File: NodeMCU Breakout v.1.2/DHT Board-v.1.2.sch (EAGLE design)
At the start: 17 parts, among them IC1 74HCT125N

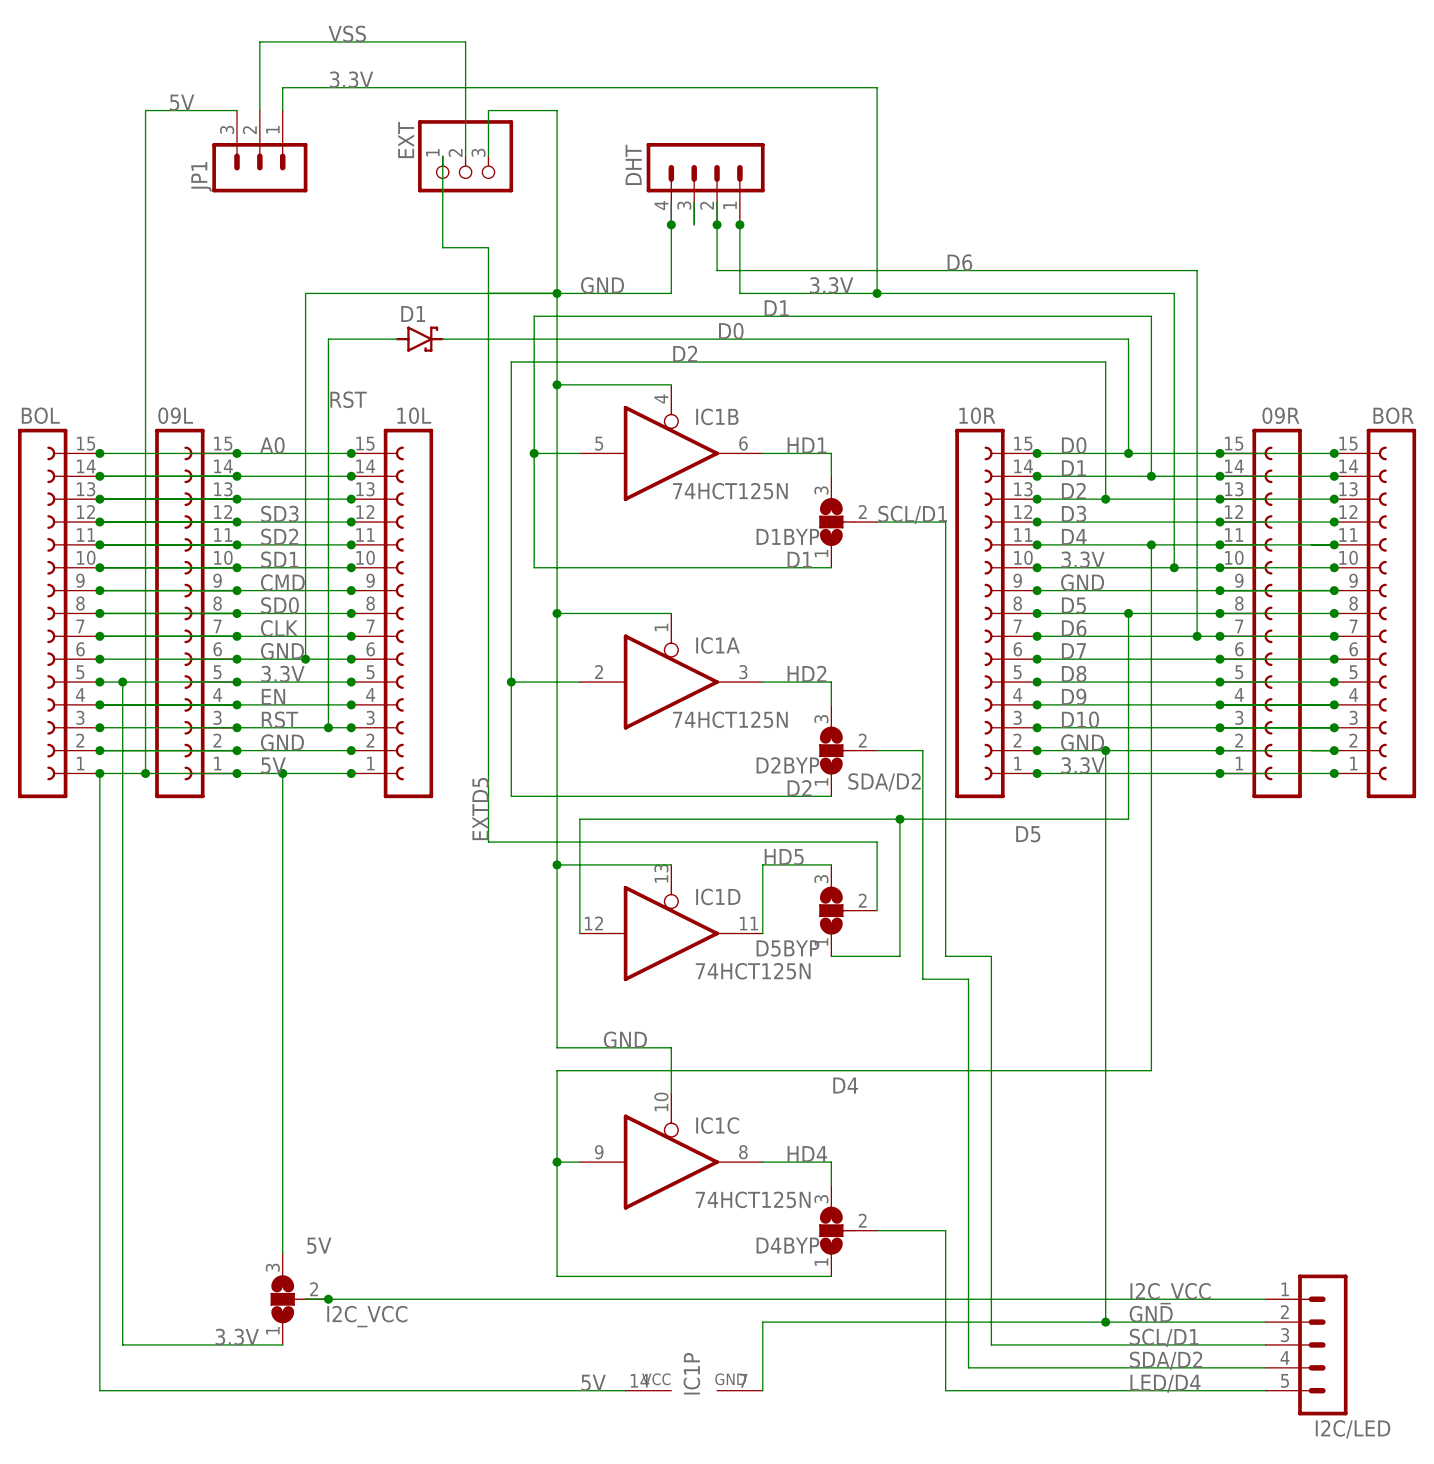
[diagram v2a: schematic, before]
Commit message: 2/2/19(BK): Updated rev 1.2 to final:
-Removed I2C_VCC Solder jumper and added 6th pin to the header (both 3.3v & 5v are brought out)
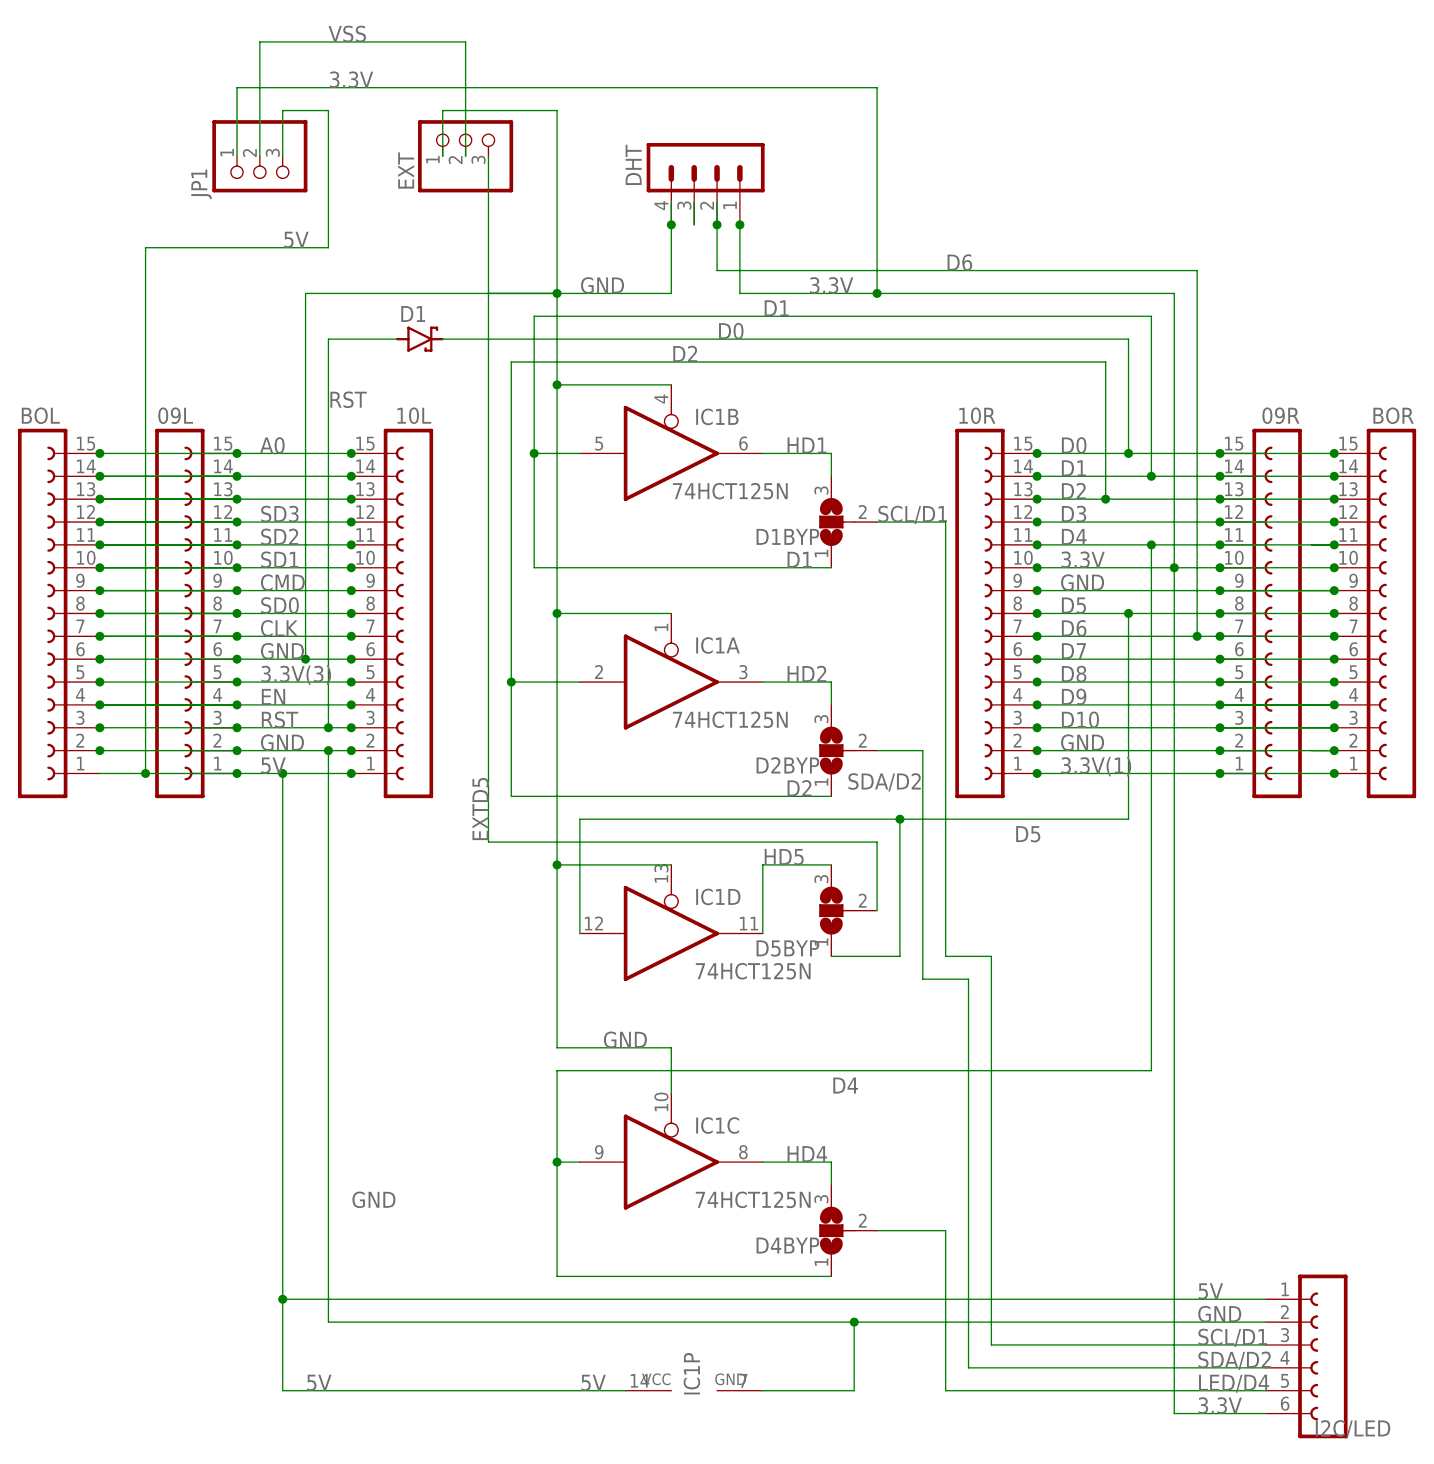
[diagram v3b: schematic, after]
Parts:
- removed I2C_VCC: (no value), jumper:SJ2W
- EXT: device pinhead:PINHD-1X3 -> pinhead:PINHD-1X3/90
- I2C/LED: device con-lstb:MA05-1 -> con-lsta:FE06-1
- JP1: device con-lstb:MA03-1 -> pinhead:PINHD-1X3
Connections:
- removed net I2C_VCC: I2C/LED.1, I2C_VCC.2
- new net 3.3V(1): 09R.1, 10R.1, BOR.1
- new net 3.3V(3): 09L.5, 10L.5, BOL.5
- net 3.3V: now also I2C/LED.6; no longer 09L.5, 09R.1, 10L.5, 10R.1, BOL.5, BOR.1, I2C_VCC.1
- net 5V: now also I2C/LED.1; no longer I2C_VCC.3
- net EXTD5: now also EXT.3; no longer EXT.1
- net GND: now also EXT.1; no longer EXT.3
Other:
- moved on the sheet: EXT
